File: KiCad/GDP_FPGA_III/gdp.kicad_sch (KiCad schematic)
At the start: 41 parts, among them J1 NKC-Bus, J2 Mini-DIN-6, J3 Mini-DIN-6, J4 AudioJack3, J5 SD_Card, U2 74LVC8T245 / 74LVXC3245, U3 74LVC8T245 / 74LVXC3245, U4 74LVC8T245 / 74LVXC3245

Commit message: some updates
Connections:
- net GND: now also J4.S; no longer J4.T
- net at C10.1, J4.R, R10.2: now also J4.T; no longer J4.S

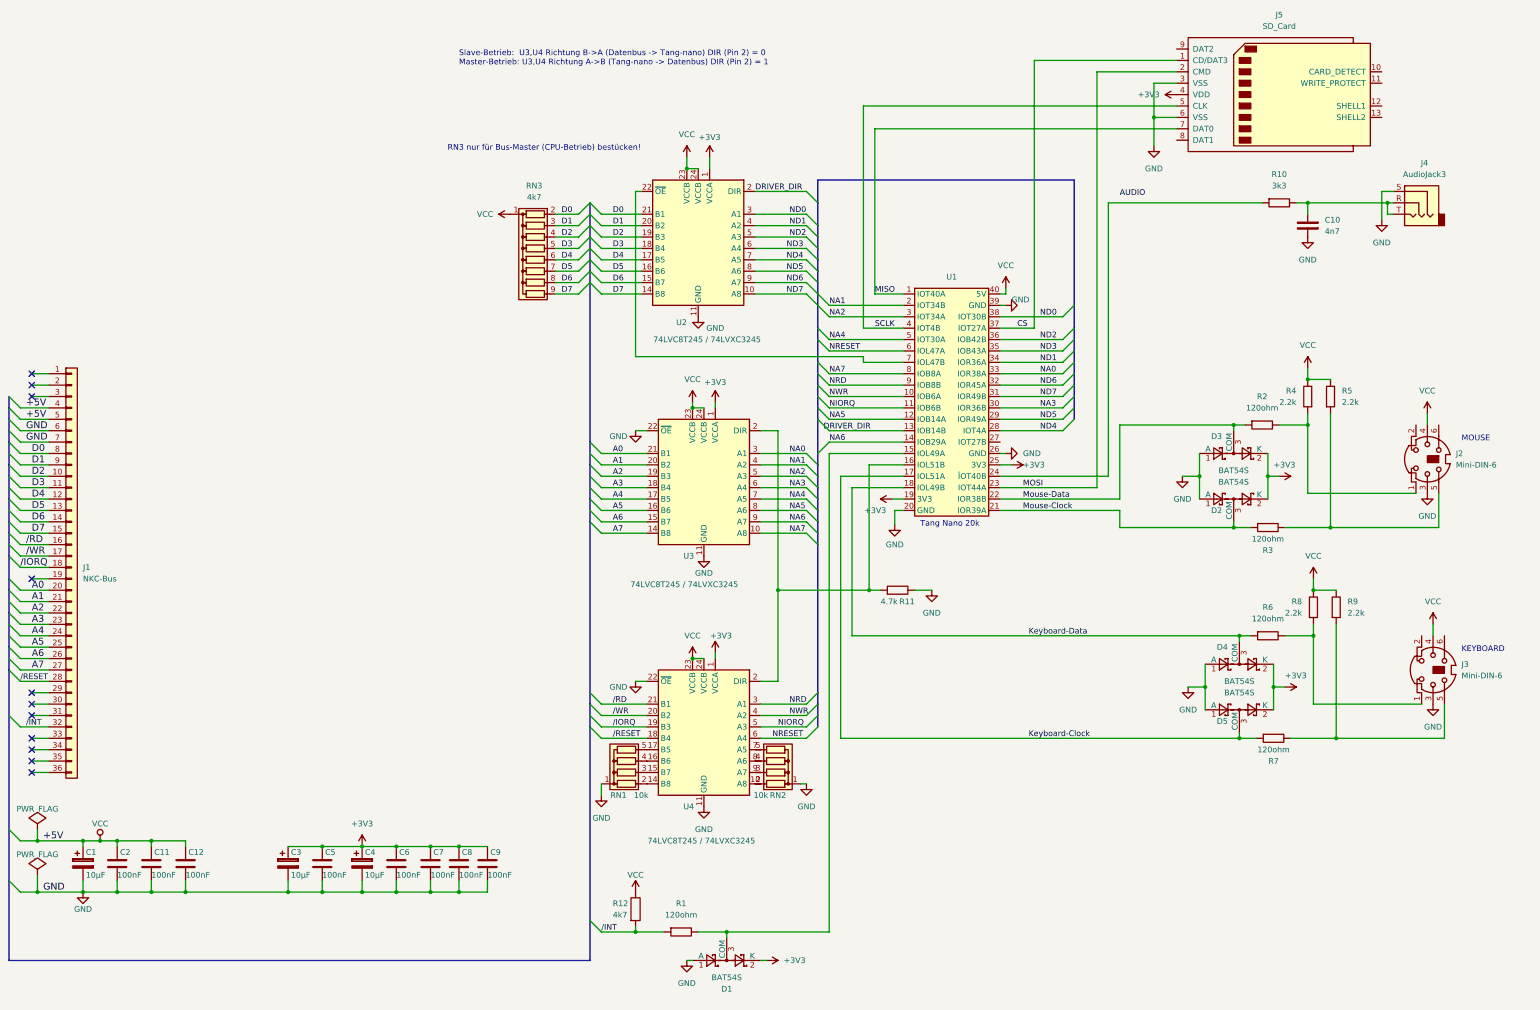
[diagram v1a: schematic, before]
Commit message: Added Schematic for NKC_SOC with Ethernet Phy
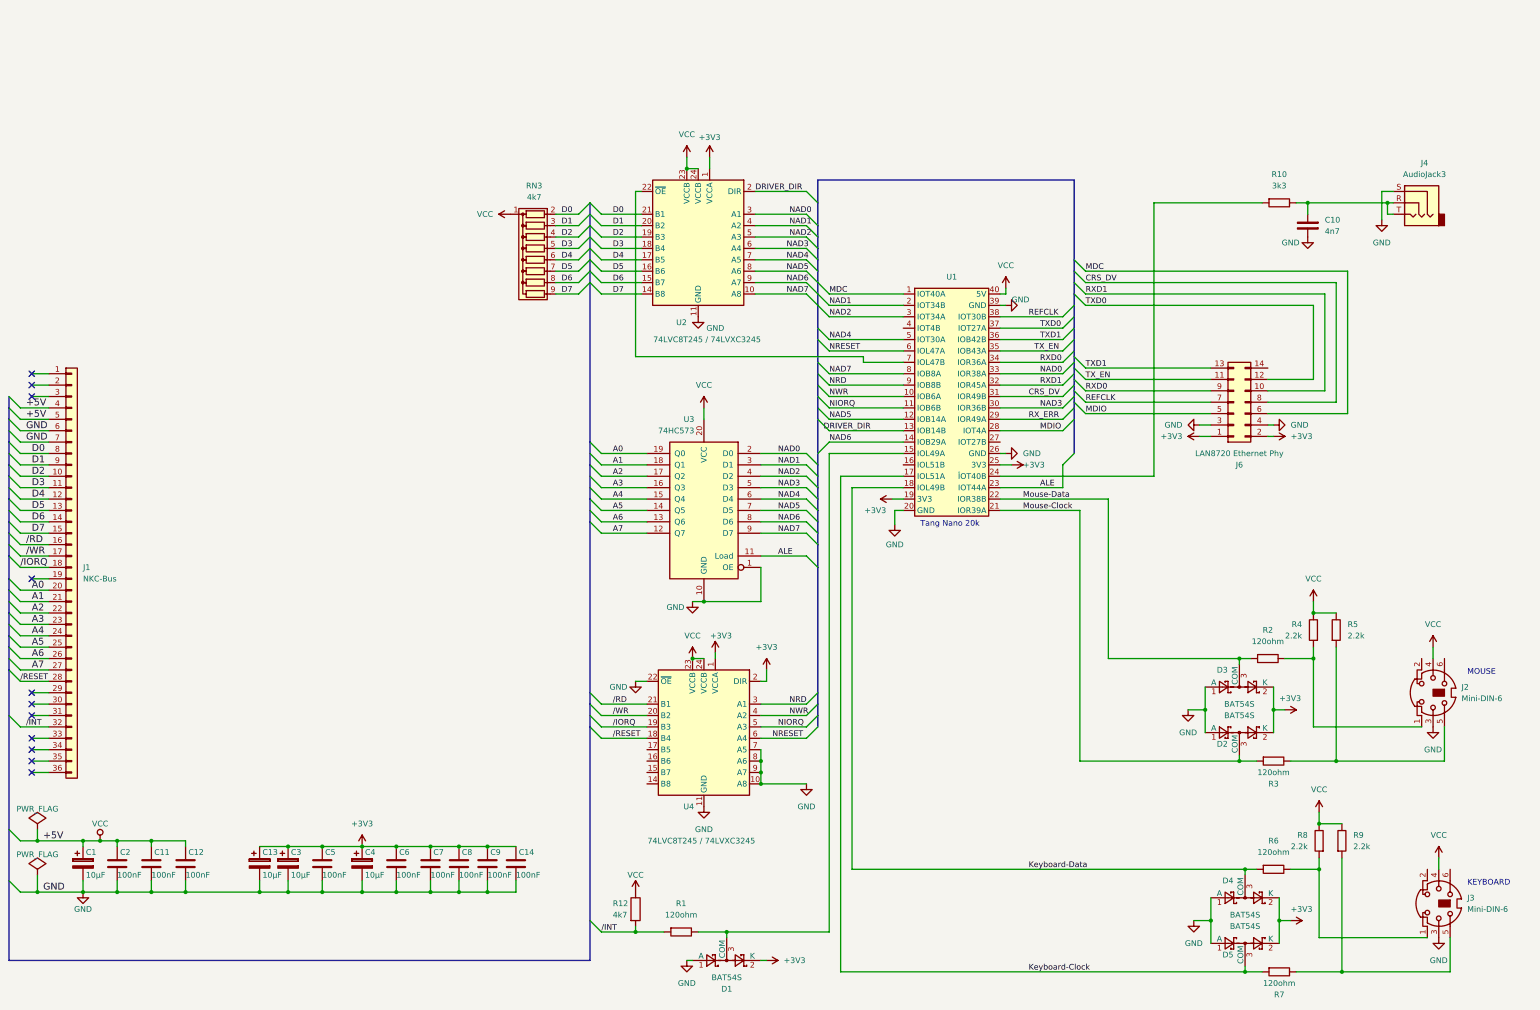
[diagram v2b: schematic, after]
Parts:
- removed J5: SD_Card, symbol Connector:SD_Card
- removed R11: 4.7k, Resistor_THT:R_Axial_DIN0207_L6.3mm_D2.5mm_P10.16mm_Horizontal, symbol PCM_SL_Resistors:2.2k
- removed RN1, RN2: 10k, Resistor_THT:R_Array_SIP5, symbol Device:R_Network04
- removed U3: 74LVC8T245 / 74LVXC3245, Package_SO:TSSOP-24_4.4x7.8mm_P0.65mm, symbol Logic_LevelTranslator:SN74AVC8T245PW
- added C13: 10µF, Capacitor_THT:CP_Radial_D5.0mm_P2.50mm, symbol ioe_enh-rescue:CP
- added C14: 100nF, Capacitor_THT:C_Disc_D5.0mm_W2.5mm_P5.00mm, symbol ioe_enh-rescue:C
- added J6: LAN8720 Ethernet Phy, symbol Connector_Generic:Conn_02x07_Odd_Even
- added U3: 74HC573, symbol 74xx:74LS573
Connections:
- net +3V3: now also U4.2 (DIR), C13.1, C14.1, J6.1 (Pin_1), J6.2 (Pin_2)
- net A0: now also U3.19 (Q0)
- net A1: now also U3.18 (Q1)
- net A2: now also U3.17 (Q2)
- net A3: now also U3.16 (Q3)
- net A4: now also U3.15 (Q4)
- net A5: now also U3.14 (Q5)
- net A6: now also U3.13 (Q6)
- net A7: now also U3.12 (Q7)
- net GND: now also U4.10 (A8), U4.7 (A5), U4.8 (A6), U4.9 (A7), C13.2, C14.2, J6.3 (Pin_3), J6.4 (Pin_4), U3.1 (OE), U3.10 (GND)
- net VCC: now also U3.20 (VCC)
- net at U1.16 (IOL51B): no longer U4.2 (DIR)
- net CS renamed TXD0
- net TXD0: now also J6.12 (Pin_12)
- net MISO renamed MDC
- net MDC: now also J6.6 (Pin_6)
- net MOSI renamed ALE
- net ALE: now also U3.11 (Load)
- net NA0 renamed NAD0
- net NAD0: now also U2.3 (A1), U3.2 (D0)
- net NA1 renamed NAD1
- net NAD1: now also U2.4 (A2), U3.3 (D1)
- net NA2 renamed NAD2
- net NAD2: now also U2.5 (A3), U3.4 (D2)
- net NA3 renamed NAD3
- net NAD3: now also U2.6 (A4), U3.5 (D3)
- net NA4 renamed NAD4
- net NAD4: now also U2.7 (A5), U3.6 (D4)
- net NA5 renamed NAD5
- net NAD5: now also U2.8 (A6), U3.7 (D5)
- net NA6 renamed NAD6
- net NAD6: now also U2.9 (A7), U3.8 (D6)
- net NA7 renamed NAD7
- net NAD7: now also U2.10 (A8), U3.9 (D7)
- net ND0 renamed REFCLK
- net REFCLK: now also J6.7 (Pin_7); no longer U2.3 (A1)
- net ND1 renamed RXD0
- net RXD0: now also J6.9 (Pin_9); no longer U2.4 (A2)
- net ND2 renamed TXD1
- net TXD1: now also J6.13 (Pin_13); no longer U2.5 (A3)
- net ND3 renamed TX_EN
- net TX_EN: now also J6.11 (Pin_11); no longer U2.6 (A4)
- net ND4 renamed MDIO
- net MDIO: now also J6.5 (Pin_5); no longer U2.7 (A5)
- net ND5 renamed RX_ERR
- net RX_ERR: no longer U2.8 (A6)
- net ND6 renamed RXD1
- net RXD1: now also J6.10 (Pin_10); no longer U2.9 (A7)
- net ND7 renamed CRS_DV
- net CRS_DV: now also J6.8 (Pin_8); no longer U2.10 (A8)
- net SCLK: no longer names the net of U1.4 (IOT4B)
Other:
- note removed: "RN3 nur für Bus-Master (CPU-Betrieb) bestücken!"
- note removed: "Slave-Betrieb: U3,U4 Richtung B->A (Datenbus -> Tang-nano) DIR (Pin 2) = 0 Master-Betrieb: U3,U4 Richtung A->B (Tang-nano -> Datenbus) DIR (Pin 2) = 1"
- title: GDP FPGA III -> Tang Nano SOC
- moved on the sheet: D2, D3, D4, D5, J2, J3, R2, R3, R4, R5, R6, R7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
